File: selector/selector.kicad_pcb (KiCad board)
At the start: 2 copper layers, 90 x 67 mm, 18 parts, among them K1 G6S-2F-5DC, K2 G6S-2F-5DC, K3 G6S-2F-5DC, K4 G6S-2F-5DC, K5 G6S-2F-5DC, X1 I2C, X2 OUTPUT, X3 POWER

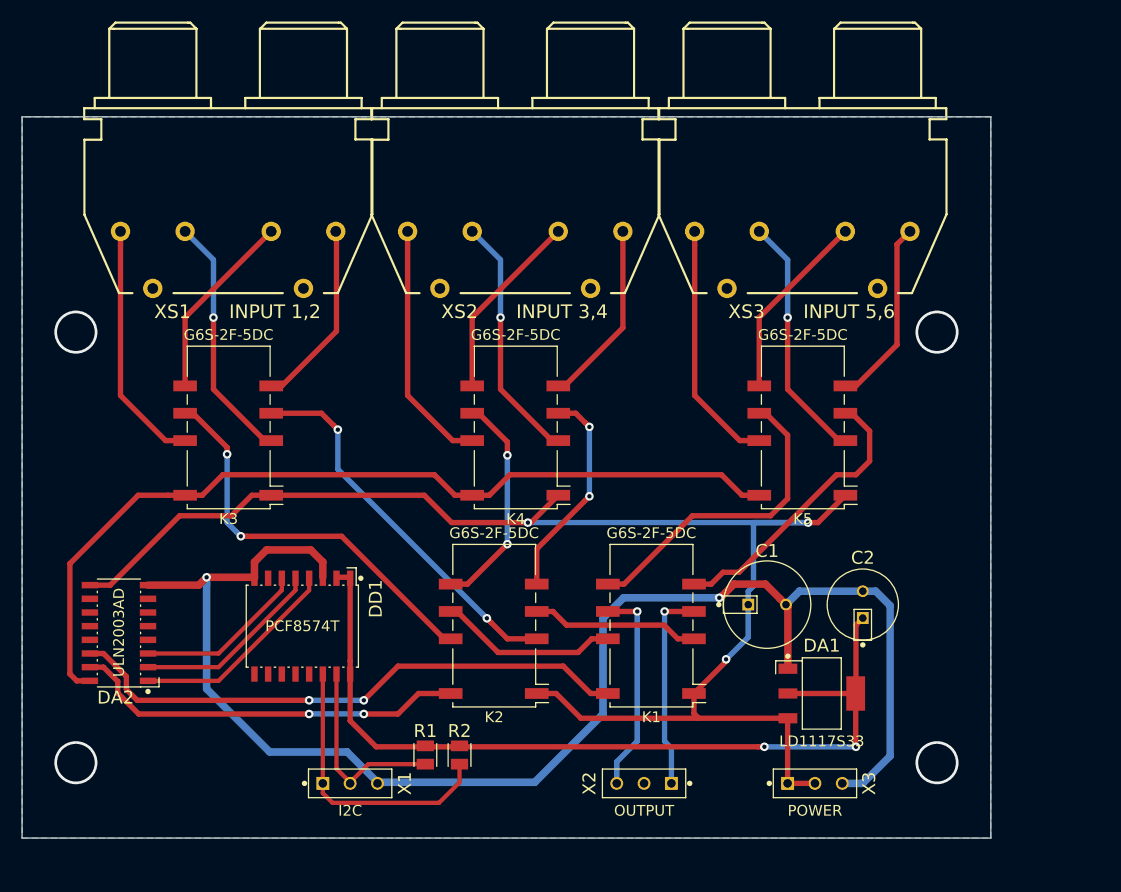
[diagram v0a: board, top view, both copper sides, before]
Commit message: Fixed selector PCB, relays on different ULN2003 lines, mainboard pcb
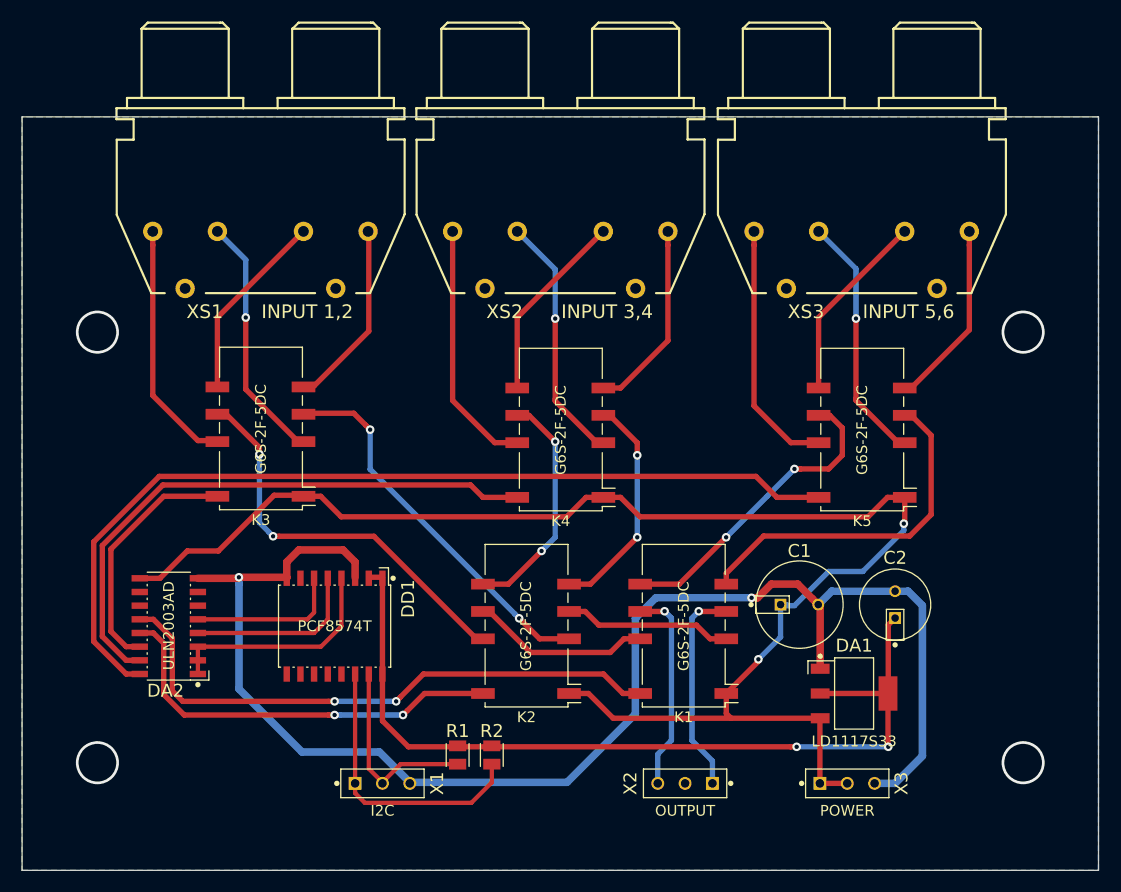
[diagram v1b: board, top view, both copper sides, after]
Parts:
- moved K5 5.52 mm to (144.7, 81.5)
- moved XS3 5.52 mm to (144.7, 63.1)
- moved DA2 4.68 mm to (80.3, 99.8)
- moved K4 4.19 mm to (116.7, 81.5)
- moved XS2 4.19 mm to (116.7, 63.1)
- moved X2 3.81 mm to (128.3, 114.4)
- moved K3 3.00 mm to (88.8, 81.4)
- moved C1 3.00 mm to (138.9, 97.8)
- moved C2 3.00 mm to (147.8, 97.8)
- moved DA1 3.00 mm to (144.0, 106.0)
- moved DD1 3.00 mm to (95.7, 99.8)
- moved K1 3.00 mm to (128.1, 99.7)
- moved K2 3.00 mm to (113.5, 99.7)
- moved R1 3.00 mm to (107.1, 111.8)
- moved R2 3.00 mm to (110.3, 111.8)
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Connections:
- DA2 pad 12: Net-(DA2-Pad12) -> /IN_2
- DA2 pad 13: Net-(DA2-Pad13) -> /IN_1
- DA2 pad 14: /IN_2 -> /IN_0C
- DA2 pad 15: /IN_1 -> /IN_0B
- DA2 pad 16: /IN_0 -> /IN_0A
- DA2 pad 2: Net-(DA2-Pad2) -> Net-(DA2-Pad1)
- DA2 pad 3: Net-(DA2-Pad3) -> Net-(DA2-Pad1)
- DD1 pad 5: Net-(DA2-Pad2) -> Net-(DA2-Pad4)
- DD1 pad 6: Net-(DA2-Pad3) -> Net-(DA2-Pad5)
- K3 pad 10: /IN_0 -> /IN_0C
- K4 pad 10: /IN_0 -> /IN_0B
- K5 pad 10: /IN_0 -> /IN_0A
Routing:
- net /IN_0A: track 0.00 -> 85.5 mm
- net /IN_0: track 82.6 -> 0.00 mm
- net /IN_0B: track 0.00 -> 54.2 mm
- net /IN_0C: track 0.00 -> 22.8 mm
- net Net-(DA2-Pad2): track 17.8 -> 0.00 mm
- net Net-(DA2-Pad4): track 0.00 -> 16.4 mm
- net Net-(DA2-Pad3): track 16.0 -> 0.00 mm
- net Net-(DA2-Pad5): track 0.00 -> 14.2 mm
- net Net-(K1-Pad5): track 26.8 -> 32.9 mm
- net +5V: track 138.1 -> 140.4 mm, vias 3 -> 2
- net /IN_1: track 36.7 -> 38.6 mm
- net GND: track 138.4 -> 136.5 mm
- net Net-(DA2-Pad1): track 19.6 -> 21.1 mm
- net /IN_2: track 53.0 -> 54.3 mm
- net Net-(K2-Pad6): track 20.7 -> 21.9 mm
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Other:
- board size 90 x 67 mm -> 100 x 70 mm

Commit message: Film caps on MB, new powering scheme, opamp replaced
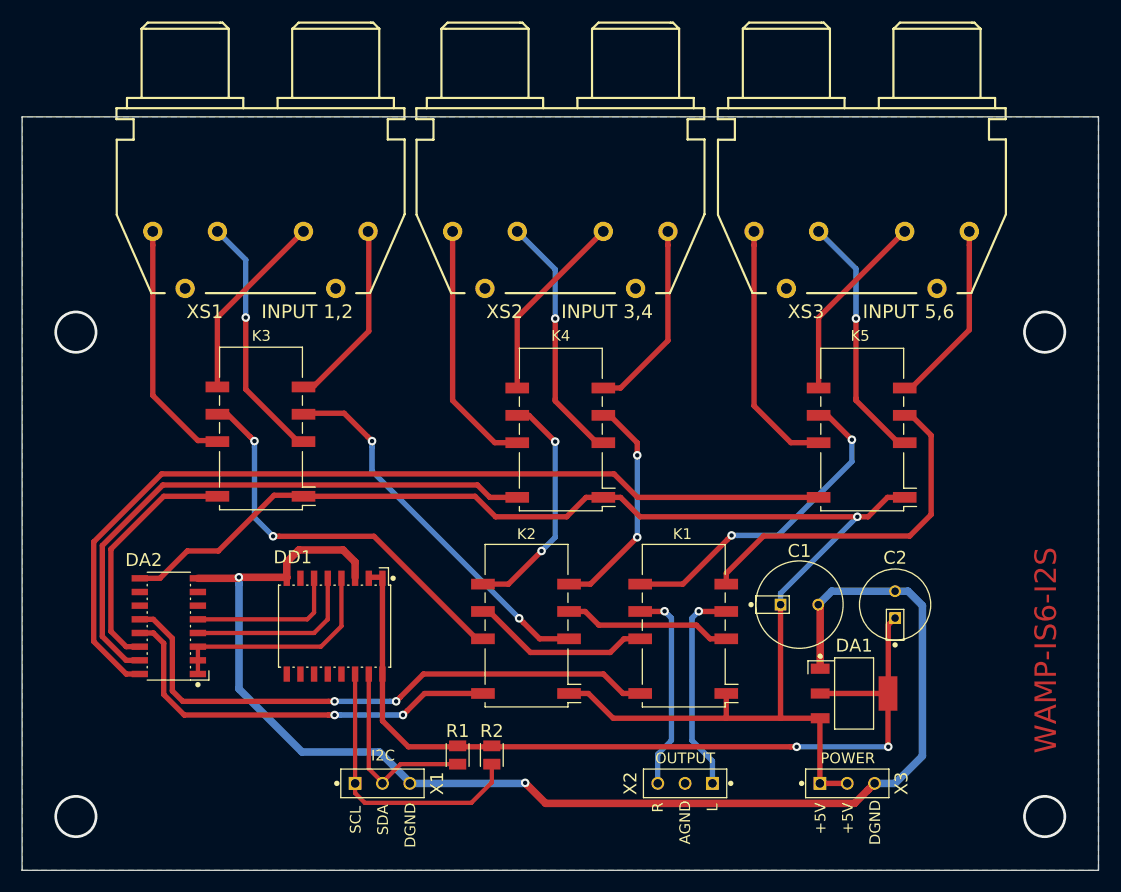
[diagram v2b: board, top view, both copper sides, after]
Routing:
- net GND: track 136.5 -> 129.7 mm
- net +5V: track 140.4 -> 134.7 mm, vias 2 -> 1
- net Net-(K1-Pad6): track 29.0 -> 30.4 mm
- net Net-(K2-Pad3): track 35.5 -> 35.0 mm
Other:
- board text added: "+5V"
- board text added: "AGND"
- board text added: "DGND"
- board text added: "L"
- board text added: "R"
- board text added: "SCL"
- board text added: "SDA"
- board text added: "WAMP-IS6-I2S"

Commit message: Headphone amp added, minor MB fixes
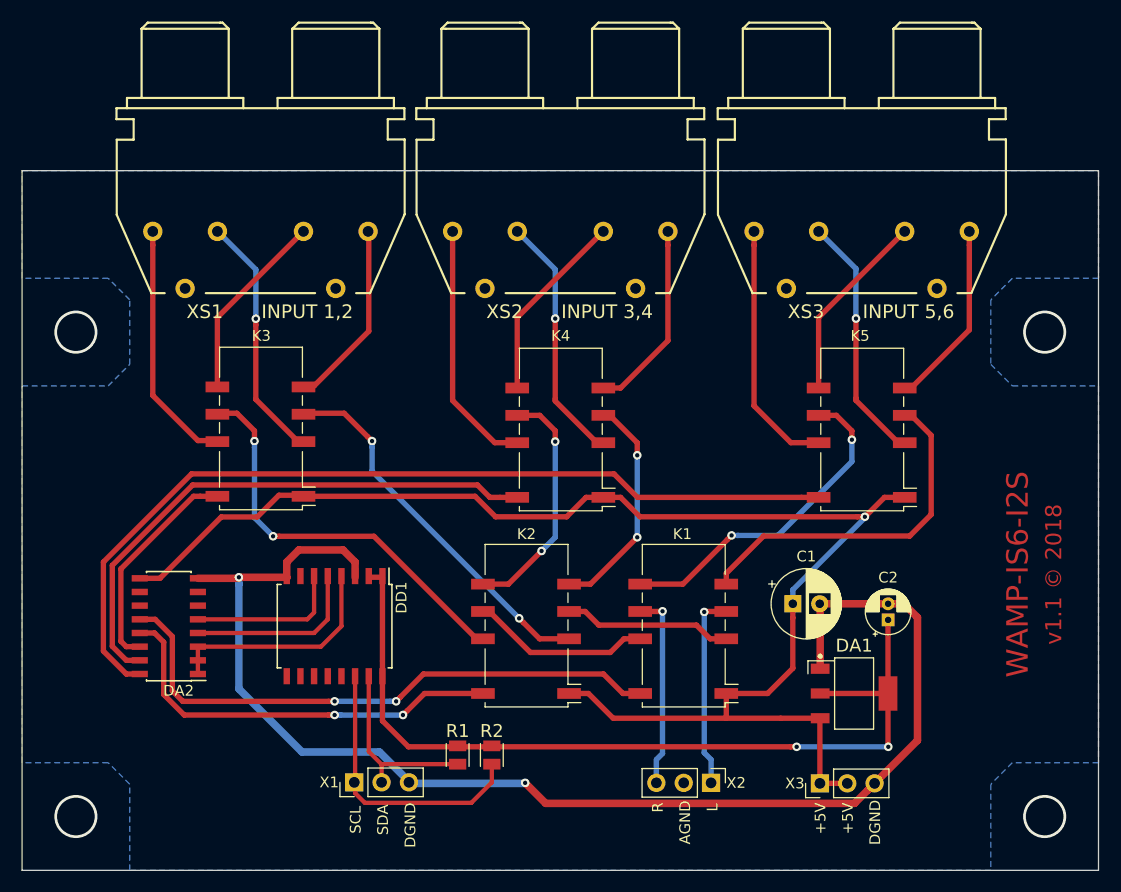
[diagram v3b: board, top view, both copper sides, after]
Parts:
- C1: footprint WAMP:CAPPRD350W50D800H800N -> Capacitor_THT:CP_Radial_D6.3mm_P2.50mm
- C2: footprint WAMP:CAPPRD250W50D650H1300N -> Capacitor_THT:CP_Radial_D4.0mm_P1.50mm
- DA2: footprint WAMP:SOIC127P600X175-16N -> Package_SO:SOIC-16_3.9x9.9mm_P1.27mm
- DD1: footprint WAMP:SOIC127P940X245-16N -> Package_SO:SOIC-16W_7.5x10.3mm_P1.27mm
- X1, X2, X3: footprint WAMP:CON_CONN_BL_03X01 -> Connector_PinHeader_2.54mm:PinHeader_1x03_P2.54mm_Vertical
- moved X1 2.62 mm to (97.5, 114.3)
- moved X3 2.54 mm to (140.8, 114.4)
- moved X2 2.41 mm to (130.7, 114.3)
- moved C2 1.56 mm to (147.1, 99.2), turned to 90 degrees
- moved C1 0.62 mm to (138.3, 97.7), turned to 0 degrees
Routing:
- net GND: track 129.7 -> 126.2 mm
- net /IN_0C: track 22.8 -> 20.4 mm
- net /IN_0B: track 54.2 -> 51.8 mm
- net /IN_0A: track 85.6 -> 83.3 mm
- net +5V: track 134.7 -> 137.0 mm
- net Net-(K1-Pad4): track 19.6 -> 18.2 mm
- net Net-(DD1-Pad15): track 18.4 -> 17.4 mm
- net Net-(K1-Pad7): track 19.1 -> 18.3 mm
- net Net-(K2-Pad6): track 21.9 -> 22.5 mm
- net Net-(K2-Pad8): track 37.5 -> 38.1 mm
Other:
- board size 100 x 70 mm -> 100 x 65 mm
- board text added: "v1.1 © 2018"
